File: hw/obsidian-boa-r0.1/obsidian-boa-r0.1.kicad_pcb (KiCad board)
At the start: 4 copper layers, 35.6 x 17.8 mm, 79 parts, among them J1 USB_C, J2 PROG, P0 0, P1 1, P10 10, P11 11, P12 12, P13 13, P14 14, P15 15, P16 16, P17 17, P18 18, P19 19, P2 2, P20 20, P21 21, P22 22, P23 23, P24 GND, P25 GND, P26 GND, P27 3V3, P28 3V3, P29 VIN, P3 3, P30 CDONE, P31 CRESET, P32 UP, P33 UP, P34 UP, P35 UP, P4 4, P5 5, P6 6, P7 7, P8 8, P9 9, SW1 TACT, U1 USBLC6-2, U2 W25Q32JVSS, U3 ESP32-S2, U4 W25Q32JVSS, U5 TPS62290, Y1 40MHz

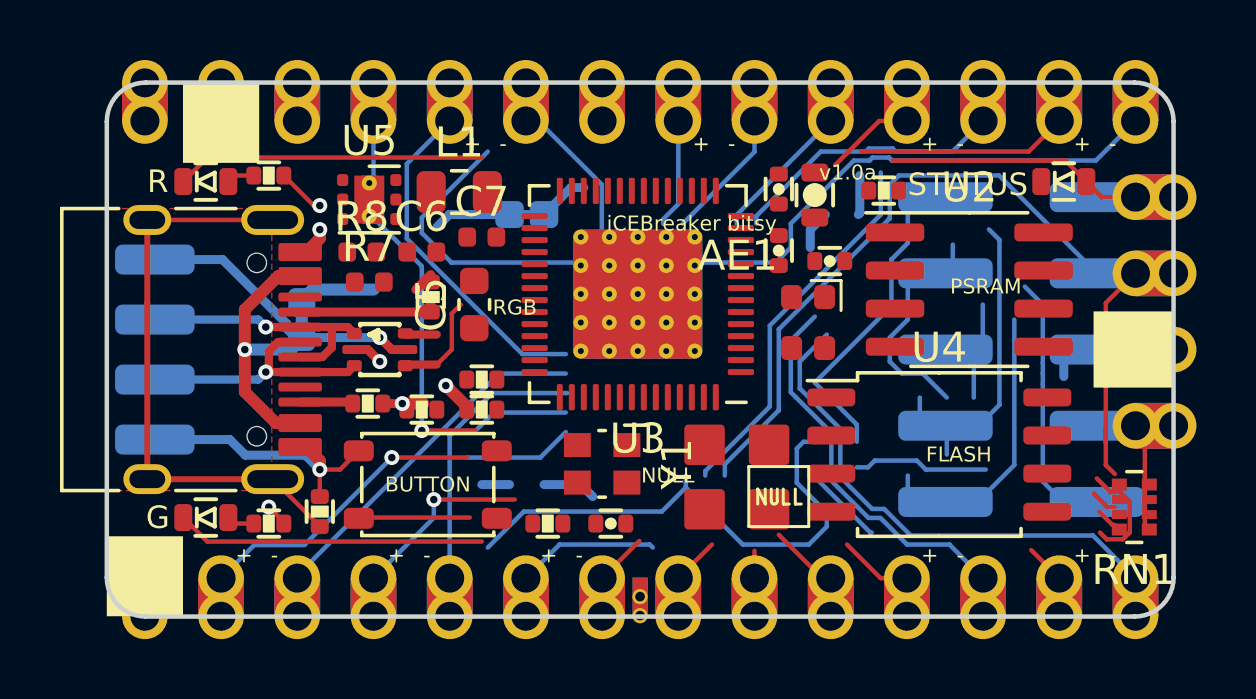
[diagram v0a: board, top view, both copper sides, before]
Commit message: hw.r0d1: Tidy up schematic, plan out layout on PCB
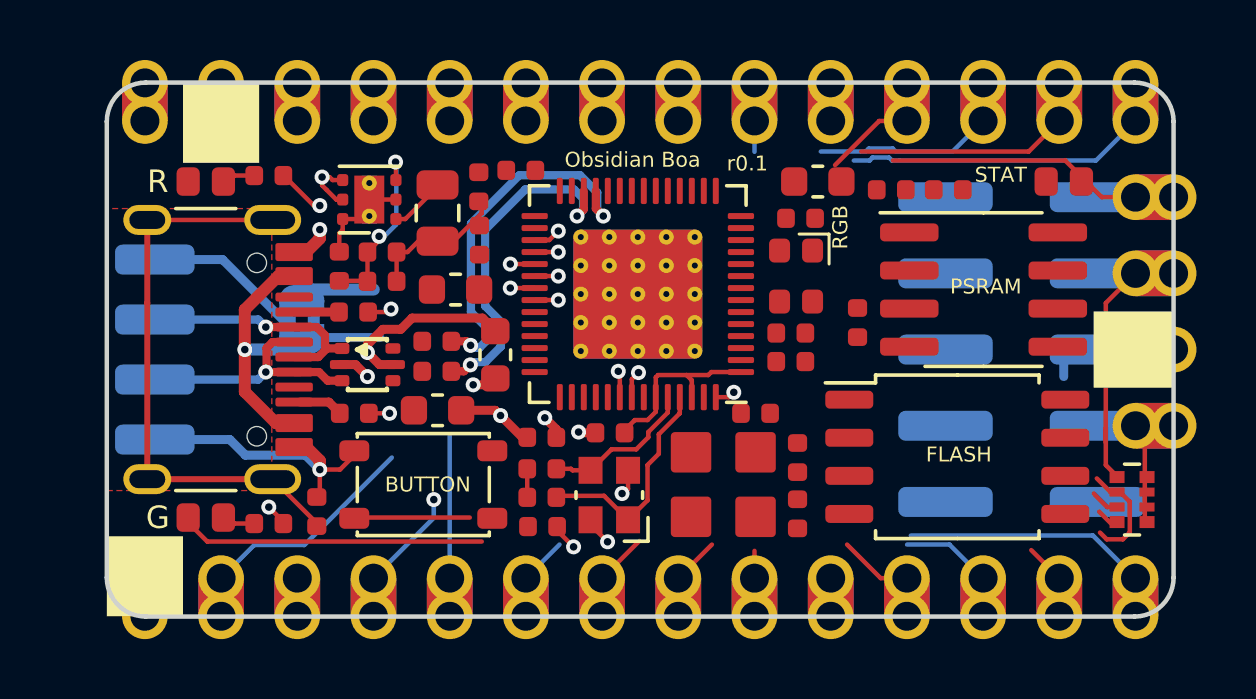
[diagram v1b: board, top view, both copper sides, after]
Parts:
- removed JP5: Jumper, pkl_jumpers:J_NC_0603_30
- removed the P5 at (117.8, 107.6)
- removed R6: 1k5, pkl_dipol:R_0402
- removed the REF** at (122.4, 104.9)
- added C1: 100n, Capacitor_SMD:C_0402_1005Metric, F.Cu at (125.0, 99.1)
- added C13: 100n, Capacitor_SMD:C_0402_1005Metric, F.Cu at (116.8, 102.8)
- added C14: 10u, Capacitor_SMD:C_0603_1608Metric, F.Cu at (123.7, 94.4)
- added C15: 100n, Capacitor_SMD:C_0402_1005Metric, F.Cu at (122.8, 100.4)
- added C2: 100n, Capacitor_SMD:C_0402_1005Metric, F.Cu at (128.1, 94.7)
- added C3: 18pF, Capacitor_SMD:C_0402_1005Metric, F.Cu at (114.5, 104.0)
- added C4: 18pF, Capacitor_SMD:C_0402_1005Metric, F.Cu at (114.5, 104.9)
- added C8: 10u, Capacitor_SMD:C_0603_1608Metric, F.Cu at (111.0, 102.0)
- added FB1: 240R, Inductor_SMD:L_0402_1005Metric, F.Cu at (113.8, 94.0)
- added FB2: 240R, Inductor_SMD:L_0402_1005Metric, F.Cu at (122.8, 99.5)
- added FB3: 240R, Inductor_SMD:L_0402_1005Metric, F.Cu at (114.5, 102.9)
- added L2: L_Small, Inductor_SMD:L_0402_1005Metric, F.Cu at (123.0, 103.6)
- C10, C11: value 100n -> TBD; footprint pkl_dipol:C_0402 -> Capacitor_SMD:C_0402_1005Metric
- C12, C9: footprint pkl_dipol:C_0402 -> Capacitor_SMD:C_0402_1005Metric
- C19: footprint pkl_dipol:C_0603 -> Capacitor_SMD:C_0603_1608Metric
- D1, D2, D3: footprint pkl_dipol:D_0603 -> obsidian-boa:LED_0603_1608Metric_Compact
- JP1: footprint pkl_jumpers:J_NC_0603_40 -> Jumper:SolderJumper-2_P1.3mm_Bridged2Bar_RoundedPad1.0x1.5mm
- R1, R10, R11, R12, R13, R2, R3, R4, R5: footprint pkl_dipol:R_0402 -> Resistor_SMD:R_0402_1005Metric
- RN1: value R_Network04_Split -> 10k
- moved C19 12.4 mm to (111.6, 98.0), turned to 180 degrees
- moved C12 10.4 mm to (112.4, 96.3), turned to -90 degrees
- moved C11 8.49 mm to (123.0, 105.5), turned to -90 degrees
- moved C10 5.48 mm to (121.6, 102.1), turned to 180 degrees
- moved R2 2.62 mm to (108.2, 98.8), turned to 180 degrees
- moved R4 1.97 mm to (111.0, 99.7)
- moved R5 1.97 mm to (111.0, 100.7)
- moved C5 1.82 mm to (113.0, 100.2), turned to -90 degrees
- moved C7 1.68 mm to (112.4, 94.6), turned to 90 degrees
- moved C6 1.65 mm to (109.2, 97.7), turned to 180 degrees
- moved D4 1.60 mm to (123.0, 97.5)
- moved C9 1.22 mm to (123.1, 95.6), turned to 180 degrees
- moved R7 1.09 mm to (109.2, 96.8), turned to 180 degrees
- moved Y1 1.07 mm to (116.8, 104.8), turned to 180 degrees
- moved L1 1.01 mm to (111.0, 95.5), turned to -90 degrees
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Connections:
- C10 pad 1: /VCCIO_0 -> Net-(C10-Pad1)
- C11 pad 1: +3V3 -> Net-(AE1-Pad1)
- C19 pad 1: +3V3 -> Net-(C19-Pad1)
- C9 pad 1: +3V3 -> Net-(C19-Pad1)
- R10 pad 2: /VCCIO_2 -> +3V3
- R11 pad 1: Net-(D1-PadA) -> Net-(D1-Pad2)
- R12 pad 1: Net-(D2-PadA) -> Net-(D2-Pad2)
- R13 pad 1: /CDONE -> Net-(D3-Pad2)
- RN1 pad 1: +3V3 -> /SPI_~CS
- RN1 pad 2: /SPI_~CS -> /RAM_~CS
- RN1 pad 3: /RAM_~CS -> /SPI_SCK
- RN1 pad 4: /SPI_SCK -> /~CRESET
- RN1 pad 5: (no net) -> +3V3
- RN1 pad 6: (no net) -> +3V3
- RN1 pad 7: (no net) -> +3V3
- RN1 pad 8: (no net) -> +3V3
- U3 pad 1: +3V3 -> Net-(C13-Pad1)
- U3 pad 2: Net-(U3-Pad2) -> Net-(C10-Pad1)
- U3 pad 20: +3V3 -> Net-(C19-Pad1)
- U3 pad 25: Net-(U3-Pad25) -> /USB_N
- U3 pad 26: Net-(U3-Pad26) -> /USB_P
- U3 pad 27: +3V3 -> Net-(C19-Pad1)
- U3 pad 3: +3V3 -> Net-(C14-Pad1)
- U3 pad 30: +3V3 -> Net-(C19-Pad1)
- U3 pad 4: +3V3 -> Net-(C14-Pad1)
- U3 pad 45: +3V3 -> Net-(C19-Pad1)
- U3 pad 51: +3V3 -> Net-(C13-Pad1)
- U3 pad 54: +3V3 -> Net-(C13-Pad1)
- Y1 pad 2: Net-(Y1-Pad2) -> GND
- Y1 pad 4: Net-(Y1-Pad4) -> GND
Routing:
- net /IOT_36b-~LEDR: track 40.6 -> 10.0 mm
- net /~CRESET: track 28.1 -> 9.10 mm, vias 0 -> 1
- net /IOB_13b-~LEDG: track 27.6 -> 10.3 mm
- net /IOB_0a: track 16.0 -> 0.00 mm, vias 1 -> 0
- net /CDONE: track 21.8 -> 9.23 mm
- net /USB_N: track 0.00 -> 12.4 mm, vias 0 -> 2
- net /IOB_3b_G6: track 12.0 -> 0.26 mm
- net /USB_P: track 0.00 -> 11.7 mm, vias 0 -> 2
- net /IOT_49a: track 11.4 -> 0.00 mm
- net Net-(J2-Pad8): track 10.6 -> 0.00 mm
- net Net-(J2-Pad10): track 10.6 -> 0.00 mm
- net /U0TXD: track 11.1 -> 0.88 mm, vias 0 -> 1
- net /IOB_23b: track 12.8 -> 3.00 mm
- net Net-(C13-Pad1): track 0.00 -> 8.86 mm, vias 0 -> 1
- net /IOB_25b_G3: track 16.9 -> 8.08 mm
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- removed copper zone on In2.Cu, net +1V2
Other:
- net class Default removed
- net class S50 removed
- net class USB-D90 removed
- board text added: "Obsidian Boa"
- board text added: "STAT"
- board text added: "r0.1"
- board text removed: "STATUS"
- board text removed: "iCEBreaker bitsy"

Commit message: hw.r0d1: Update routing and layout
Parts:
- added R14: 2k2, Resistor_SMD:R_0402_1005Metric, F.Cu at (122.8, 97.2)
- added R6: 2k2, Resistor_SMD:R_0402_1005Metric, F.Cu at (122.8, 98.2)
- added R9: 2k2, Resistor_SMD:R_0402_1005Metric, F.Cu at (122.8, 96.3)
- D4: footprint pkl_led:LED_TRI_2020 -> LED_SMD:LED_Lumex_SML-LX0303SIUPGUSB
- L2: value L_Small -> TBD
- moved JP1 4.98 mm to (103.4, 95.1)
- moved D4 1.63 mm to (124.6, 97.5)
- moved C15 1.50 mm to (123.7, 99.2)
- moved C9 1.49 mm to (122.7, 94.2), turned to 0 degrees
- moved FB3 1.39 mm to (113.3, 102.2)
- moved FB2 1.17 mm to (123.7, 100.2)
- moved C14 0.99 mm to (124.4, 95.1), turned to 90 degrees
- moved C10 0.78 mm to (122.4, 102.1)
- moved C1 0.61 mm to (125.2, 99.7)
- moved C3 0.08 mm to (114.4, 104.0)
- moved C4 0.08 mm to (114.4, 104.9)
- moved R10 0.08 mm to (114.5, 105.9)
- moved RN1 0.07 mm to (134.2, 105.0)
- moved C5 0.06 mm to (112.9, 100.2)
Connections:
- D1 pad 1: /IOT_36b-~LEDR -> /~LEDR
- D2 pad 1: /IOB_13b-~LEDG -> /~LEDG
- D3 pad 1: /IOB_13b-~LEDB -> /GPIO11-~LEDB
- D4 pad 1: /~RGB0 -> +3V3
- D4 pad 2: /~RGB2 -> Net-(D4-Pad2)
- D4 pad 3: +3V3 -> Net-(D4-Pad3)
- D4 pad 4: /~RGB1 -> Net-(D4-Pad4)
- J2 pad 1: /CDONE -> /GPIO0-SPI_BOOT
- J2 pad 10: Net-(J2-Pad10) -> /U0RXD
- J2 pad 2: /U0TXD -> /GPIO7
- J2 pad 4: /U0RXD -> Net-(J2-Pad4)
- J2 pad 9: /SPI_~WP~-IO2 -> /U0TXD
- P13 pad 1: /IOT_36b-~LEDR -> /GPIO11-~LEDB
- P20 pad 1: /IOT_44b -> Net-(P20-Pad1)
- P21 pad 1: /IOT_48b -> Net-(P21-Pad1)
- P22 pad 1: /IOT_49a -> /DAC_2
- P23 pad 1: /IOB_0a -> /DAC_1
- P30 pad 1: /CDONE -> /GPIO0-SPI_BOOT
- RN1 pad 1: /SPI_~CS -> /~CRESET
- RN1 pad 4: /~CRESET -> /SPI_~CS
- U3 pad 10: Net-(U3-Pad10) -> /~RGB2
- U3 pad 11: Net-(U3-Pad11) -> /~RGB1
- U3 pad 12: Net-(U3-Pad12) -> /GPIO7
- U3 pad 13: Net-(U3-Pad13) -> /IOT_38b
- U3 pad 14: Net-(U3-Pad14) -> /IOT_37a
- U3 pad 15: Net-(U3-Pad15) -> /IOT_41a
- U3 pad 16: Net-(U3-Pad16) -> /GPIO11-~LEDB
- U3 pad 17: Net-(U3-Pad17) -> /IOT_39a
- U3 pad 18: Net-(U3-Pad18) -> /IOT_42b
- U3 pad 19: Net-(U3-Pad19) -> /IOT_43a
- U3 pad 21: Net-(U3-Pad21) -> Net-(P20-Pad1)
- U3 pad 22: Net-(U3-Pad22) -> Net-(P21-Pad1)
- U3 pad 23: Net-(U3-Pad23) -> /DAC_1
- U3 pad 24: Net-(U3-Pad24) -> /DAC_2
- U3 pad 28: Net-(U3-Pad28) -> /~LEDR
- U3 pad 37: Net-(U3-Pad37) -> /~LEDG
- U3 pad 38: Net-(U3-Pad38) -> /~BTN
- U3 pad 39: Net-(U3-Pad39) -> /IOB_5b
- U3 pad 40: Net-(U3-Pad40) -> /IOB_3b_G6
- U3 pad 41: Net-(U3-Pad41) -> /IOB_2a
- U3 pad 42: Net-(U3-Pad42) -> /IOB_4a
- U3 pad 43: Net-(U3-Pad43) -> /IOB_8a
- U3 pad 44: Net-(U3-Pad44) -> /IOB_9b
- U3 pad 46: Net-(U3-Pad46) -> /IOB_16a
- U3 pad 47: Net-(U3-Pad47) -> /IOB_18a
- U3 pad 5: Net-(U3-Pad5) -> /GPIO0-SPI_BOOT
- U3 pad 50: Net-(U3-Pad50) -> /IOB_20a
- U3 pad 55: Net-(U3-Pad55) -> /IOB_23b
- U3 pad 6: Net-(U3-Pad6) -> /IOB_22a
- U3 pad 7: Net-(U3-Pad7) -> /IOB_24a
- U3 pad 8: Net-(U3-Pad8) -> /~RGB0
- U3 pad 9: Net-(U3-Pad9) -> /IOB_25b_G3
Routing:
- net /SPI_SCK: track 1.67 -> 36.3 mm, vias 1 -> 2
- net Net-(C19-Pad1): track 0.00 -> 33.0 mm, vias 0 -> 4
- net /SPI_~HLD~-IO3: track 0.91 -> 29.7 mm, vias 1 -> 2
- net /SPI_~CS: track 0.81 -> 29.3 mm, vias 1 -> 3
- net /RAM_~CS: track 3.63 -> 31.9 mm, vias 0 -> 2
- net /SPI_COPI-IO0: track 0.79 -> 28.9 mm, vias 1 -> 4
- net /SPI_CIPO-IO1: track 0.81 -> 26.9 mm, vias 1 -> 3
- net GND: track 22.2 -> 47.1 mm, vias 9 -> 20
- net /GPIO0-SPI_BOOT: track 0.00 -> 23.3 mm, vias 0 -> 1
- net /SPI_~WP~-IO2: track 1.91 -> 23.9 mm, vias 1 -> 2
- net /~LEDG: track 0.00 -> 20.8 mm, vias 0 -> 2
- net /IOB_25b_G3: track 8.08 -> 28.0 mm, vias 0 -> 2
- net /U0TXD: track 0.88 -> 20.4 mm
- net /IOB_24a: track 1.32 -> 20.5 mm, vias 0 -> 2
- net /GPIO11-~LEDB: track 0.00 -> 17.3 mm, vias 0 -> 2
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
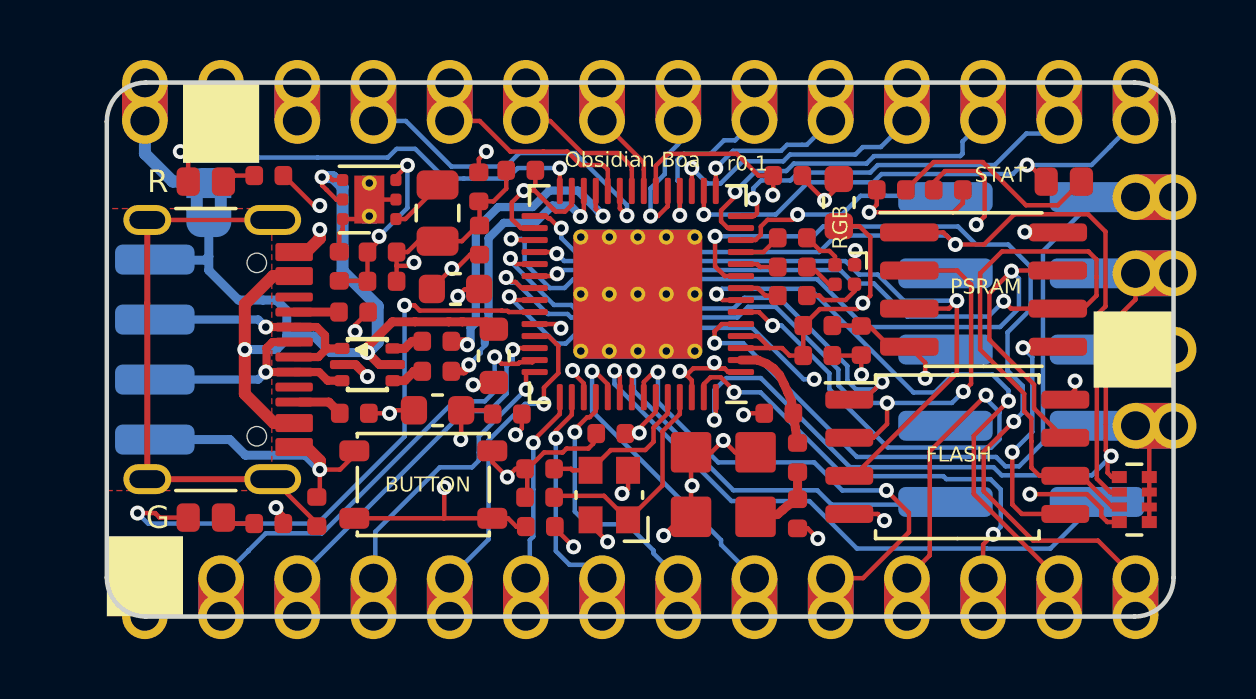
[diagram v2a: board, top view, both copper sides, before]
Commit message: hw.r0d1: Complete first pass of layout and routing
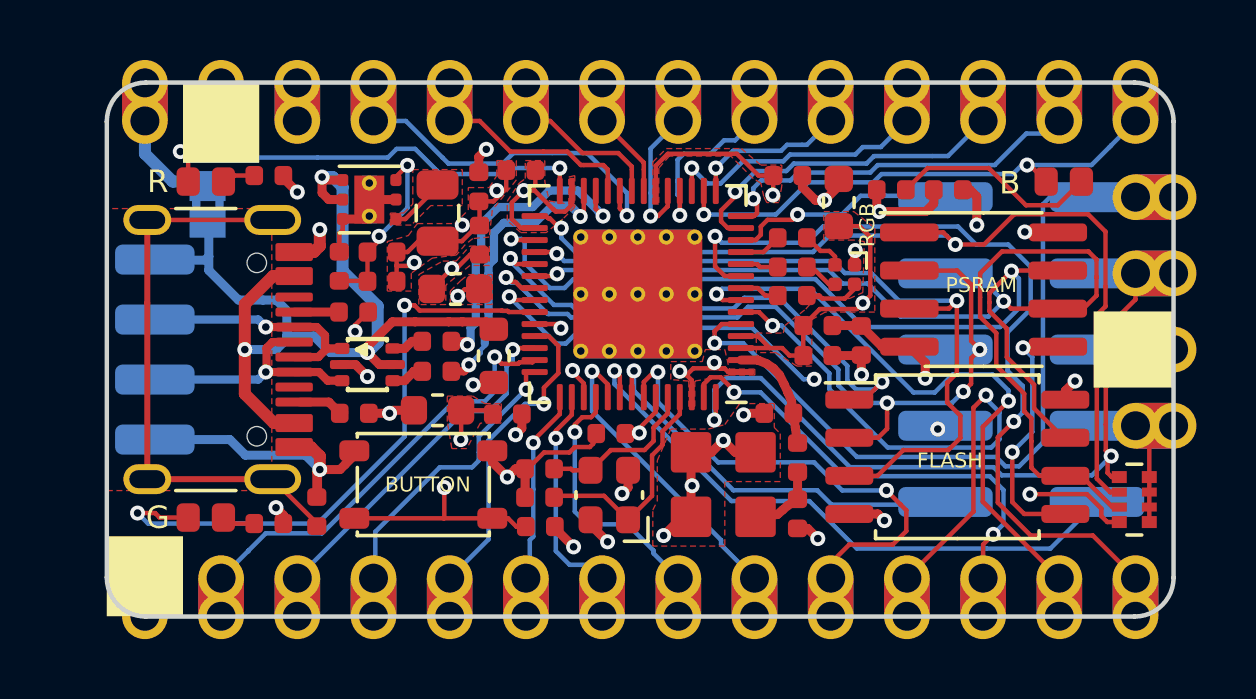
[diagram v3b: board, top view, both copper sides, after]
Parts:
- moved REF** 2.37 mm to (108.8, 101.4)
- moved REF** 2.37 mm to (106.0, 100.9)
- moved REF** 2.37 mm to (107.2, 100.9)
- moved JP1 0.07 mm to (103.4, 95.2)
- turned C2 to 0 degrees
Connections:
- net /DAC_1 renamed /GPIO17-DAC_1
- net /DAC_2 renamed /GPIO18-DAC_2
- net /GPIO0-SPI_BOOT renamed /GPIO0-BOOT
- net /IOB_16a renamed /GPIO41
- net /IOB_18a renamed /GPIO42
- net /IOB_20a renamed /GPIO45
- net /IOB_22a renamed /GPIO1
- net /IOB_23b renamed /GPIO46
- net /IOB_24a renamed /GPIO2
- net /IOB_25b_G3 renamed /GPIO4
- net /IOB_2a renamed /GPIO37
- net /IOB_3b_G6 renamed /GPIO36
- net /IOB_4a renamed /GPIO38
- net /IOB_5b renamed /GPIO35
- net /IOB_8a renamed /GPIO39
- net /IOB_9b renamed /GPIO40
- net /IOT_37a renamed /GPIO9
- net /IOT_38b renamed /GPIO8
- net /IOT_39a renamed /GPIO12
- net /IOT_41a renamed /GPIO10
- net /IOT_42b renamed /GPIO13
- net /IOT_43a renamed /GPIO14
- net /~BTN renamed /GPIO34-~BTN
- net Net-(P20-Pad1) renamed /GPIO15
- net Net-(P21-Pad1) renamed /GPIO16
- J2 pad 4: Net-(J2-Pad4) -> /SPI_SCK
- J2 pad 6: Net-(J2-Pad6) -> /SPI_CIPO-IO1
- J2 pad 8: Net-(J2-Pad8) -> /SPI_COPI-IO0
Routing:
- net /SPI_SCK: track 36.3 -> 38.7 mm
- net /SPI_~WP~-IO2: track 23.9 -> 25.6 mm
- net GND: track 47.1 -> 48.1 mm
- net /GPIO0-BOOT: track 23.3 -> 24.2 mm
- net /SPI_~CS: track 29.3 -> 29.8 mm
- net /SPI_CIPO-IO1: track 26.9 -> 27.2 mm, vias 3 -> 4
- net /SPI_COPI-IO0: vias 4 -> 5
- net +3V3: vias 10 -> 12
- added copper zone on F.Cu, net +3V3
- added copper zone on F.Cu, net GND
- added copper zone on F.Cu, net Net-(C13-Pad1)
- added copper zone on In2.Cu, net Net-(C13-Pad1)
- added copper zone on F.Cu, net Net-(C14-Pad1)
- added copper zone on F.Cu, net Net-(C19-Pad1)
- added copper zone on In2.Cu, net Net-(C19-Pad1)
- added copper zone on F.Cu, net Net-(L1-Pad1)
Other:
- board text added: "(Chance of bugs: High)"
- board text added: "35"
- board text added: "36"
- board text added: "37"
- board text added: "38"
- board text added: "39"
- board text added: "40"
- board text added: "41"
- board text added: "42"
- board text added: "45"
- board text added: "46"
- board text added: "B"
- board text added: "BOOT"
- board text added: "CIPO"
- board text added: "COPI"
- board text added: "Gnd"
- board text added: "RxD"
- board text added: "TxD"
- board text added: "Vbus"
- board text added: "by @gregdavill 2020"
- board text removed: "+"
- board text removed: "+IOB_22a 12 09"
- board text removed: "+IOB_24a 13 11"
- board text removed: "+IOB_2a 47 00"
- board text removed: "+IOB_4a 48 02"
- board text removed: "+IOB_8a 04 04"
- board text removed: "-"
- board text removed: "-IOB_23b 21 10"
- board text removed: "-IOB_5b 45 03"
- board text removed: "-IOB_9b 03 05"
- board text removed: "/"
- board text removed: "0"
- board text removed: "13 25 IOT_36b- ~LEDR"
- board text removed: "14 23 IOT_37a+"
- board text removed: "15 27 IOT_38b-"
- board text removed: "16 26 IOT_39a+"
- board text removed: "17 28 IOT_41a"
- board text removed: "18 31 IOT_42b-"
- board text removed: "19"
- board text removed: "19 32 IOT_43a+"
- board text removed: "20"
- board text removed: "20 34 IOT_44b"
- board text removed: "21"
- board text removed: "21 36 IOT_48b-"
- board text removed: "22"
- board text removed: "22 43 IOT_49a+"
- board text removed: "23"
- board text removed: "23 46 IOB_0a"
- board text removed: "3"
- board text removed: "3.3V"
- board text removed: "5"
- board text removed: "6"
- board text removed: "CDON"
- board text removed: "CDONE"
- board text removed: "CRESET"
- board text removed: "CS"
- board text removed: "F"
- board text removed: "G3 -IOB_25b 20 12"
- board text removed: "G6 -IOB_3b 44 01"
- board text removed: "IO2"
- board text removed: "IO3"
- board text removed: "IOB_16a 09 06"
- board text removed: "IOB_18a 10 07"
- board text removed: "IOB_20a 11 08"
- board text removed: "MISO"
- board text removed: "MOSI"
- board text removed: "NULL"
- board text removed: "QSPI Prog"
- board text removed: "STAT"
- board text removed: "V"
- board text removed: "VccIO0"
- board text removed: "VccIO2"
- board text removed: "Vpp2v5"
- board text removed: "bitsy"
- board text removed: "by @0xdec 2020"
- board text removed: "iCEBreaker"
- board text removed: "v1.0a"
